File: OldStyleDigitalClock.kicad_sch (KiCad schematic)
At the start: 52 parts, among them SW1 Set minutes, SW2 Set hours, U1 CD4071BM, U10 CD4026BNSR, U2 D168K, U3 CD4026BNSR, U4 D168K, U5 CD4026BNSR, U6 CD4073BM, U7 D168K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

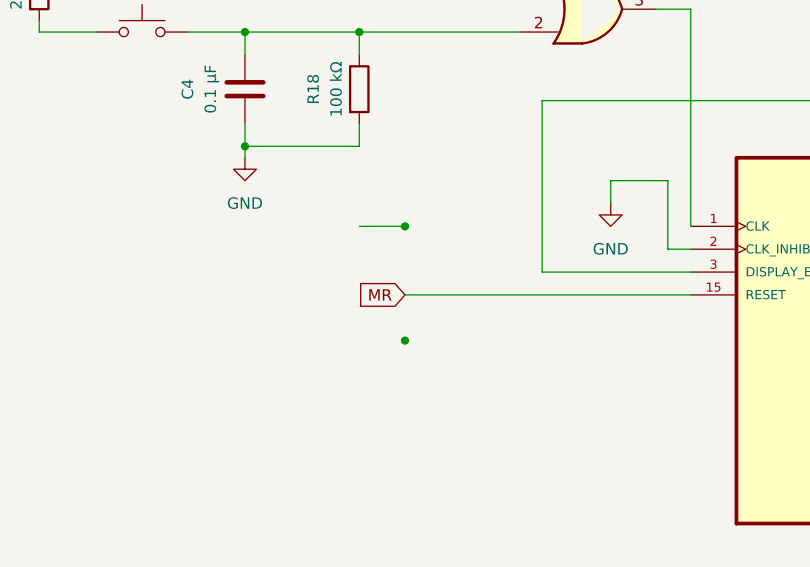
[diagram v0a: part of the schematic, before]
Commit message: Corrected Zener diode specs
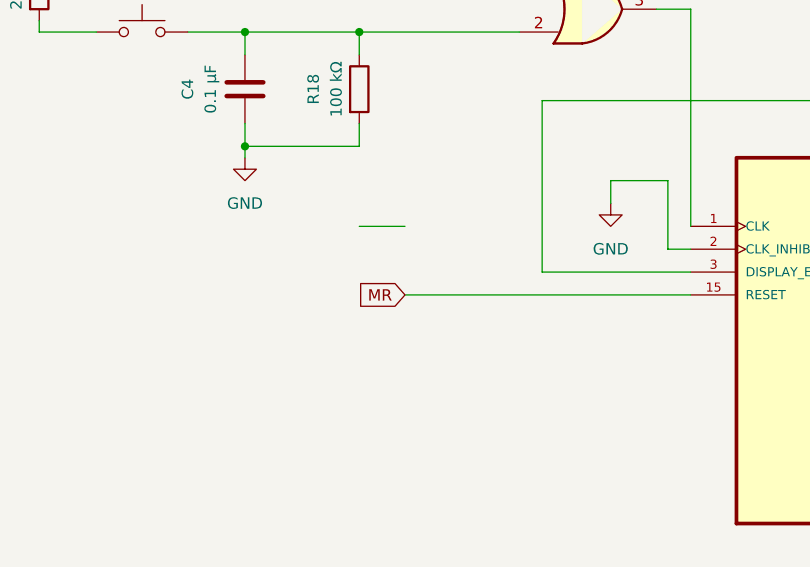
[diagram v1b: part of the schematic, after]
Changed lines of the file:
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@@
-	)
-	(junction
-		(at 134.62 171.45)
-		(diameter 0)
-		(color 0 0 0 0)
 	)
 	(junction
@@
 		(diameter 0)
 		(color 0 0 0 0)
-	)
-	(junction
-		(at 134.62 184.15)
-		(diameter 0)
-		(color 0 0 0 0)

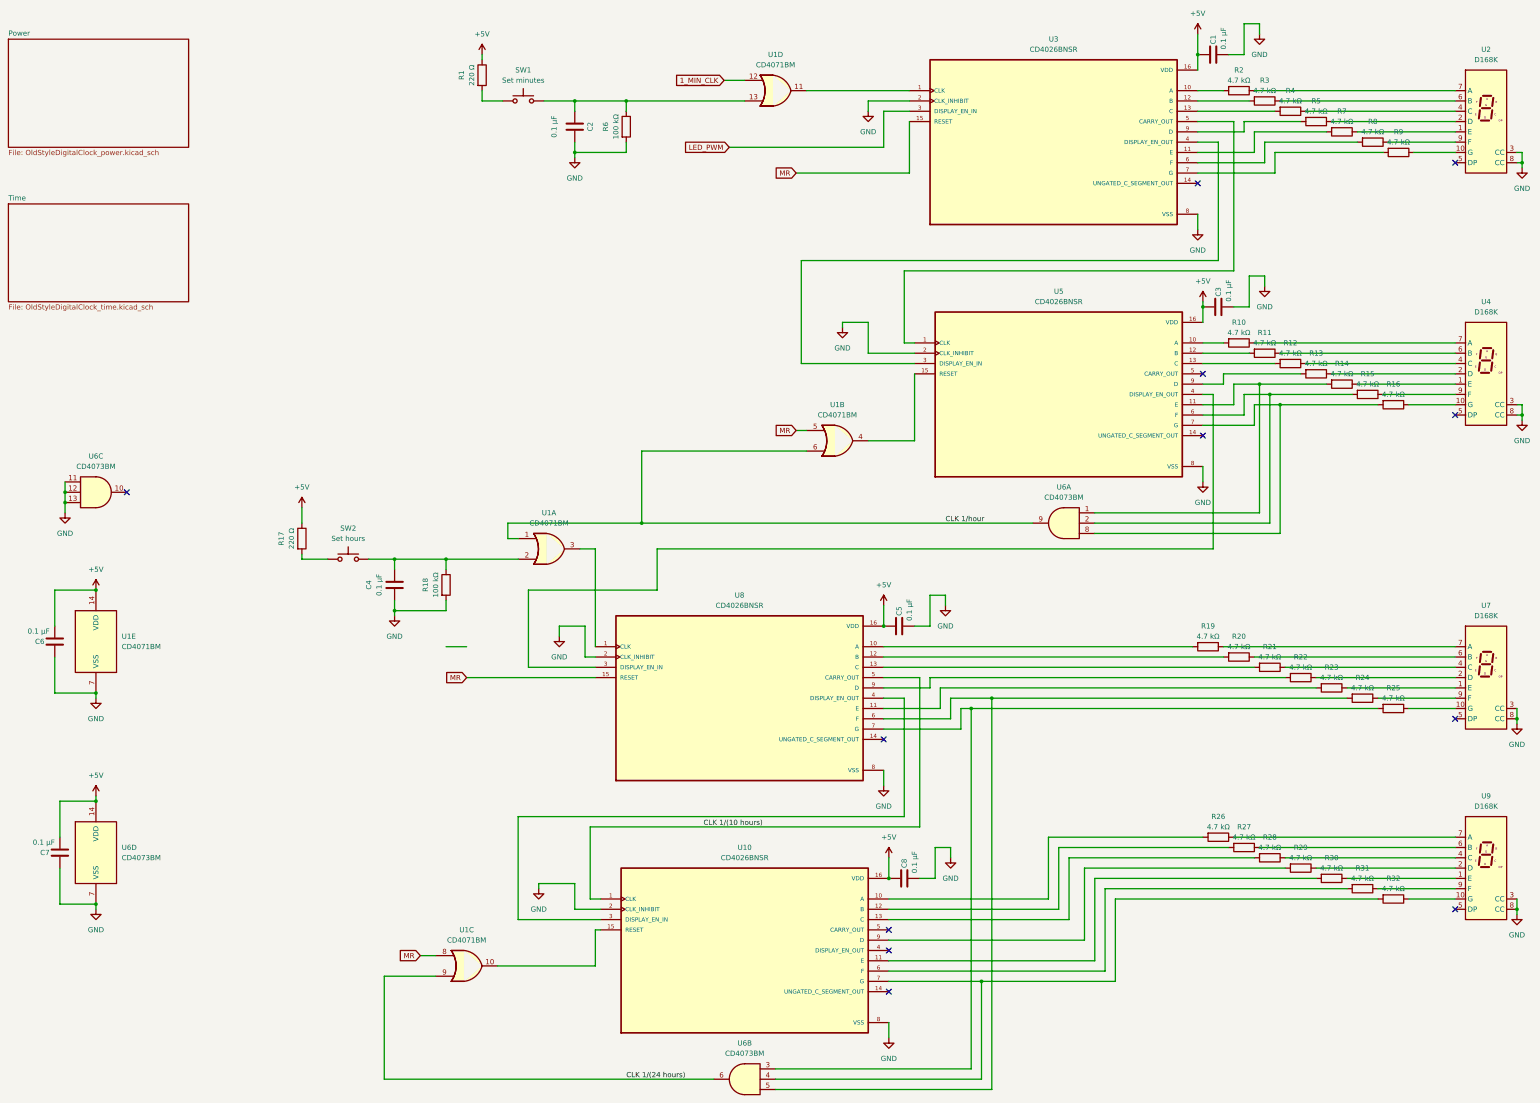
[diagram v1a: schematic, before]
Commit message: Changed units for caps
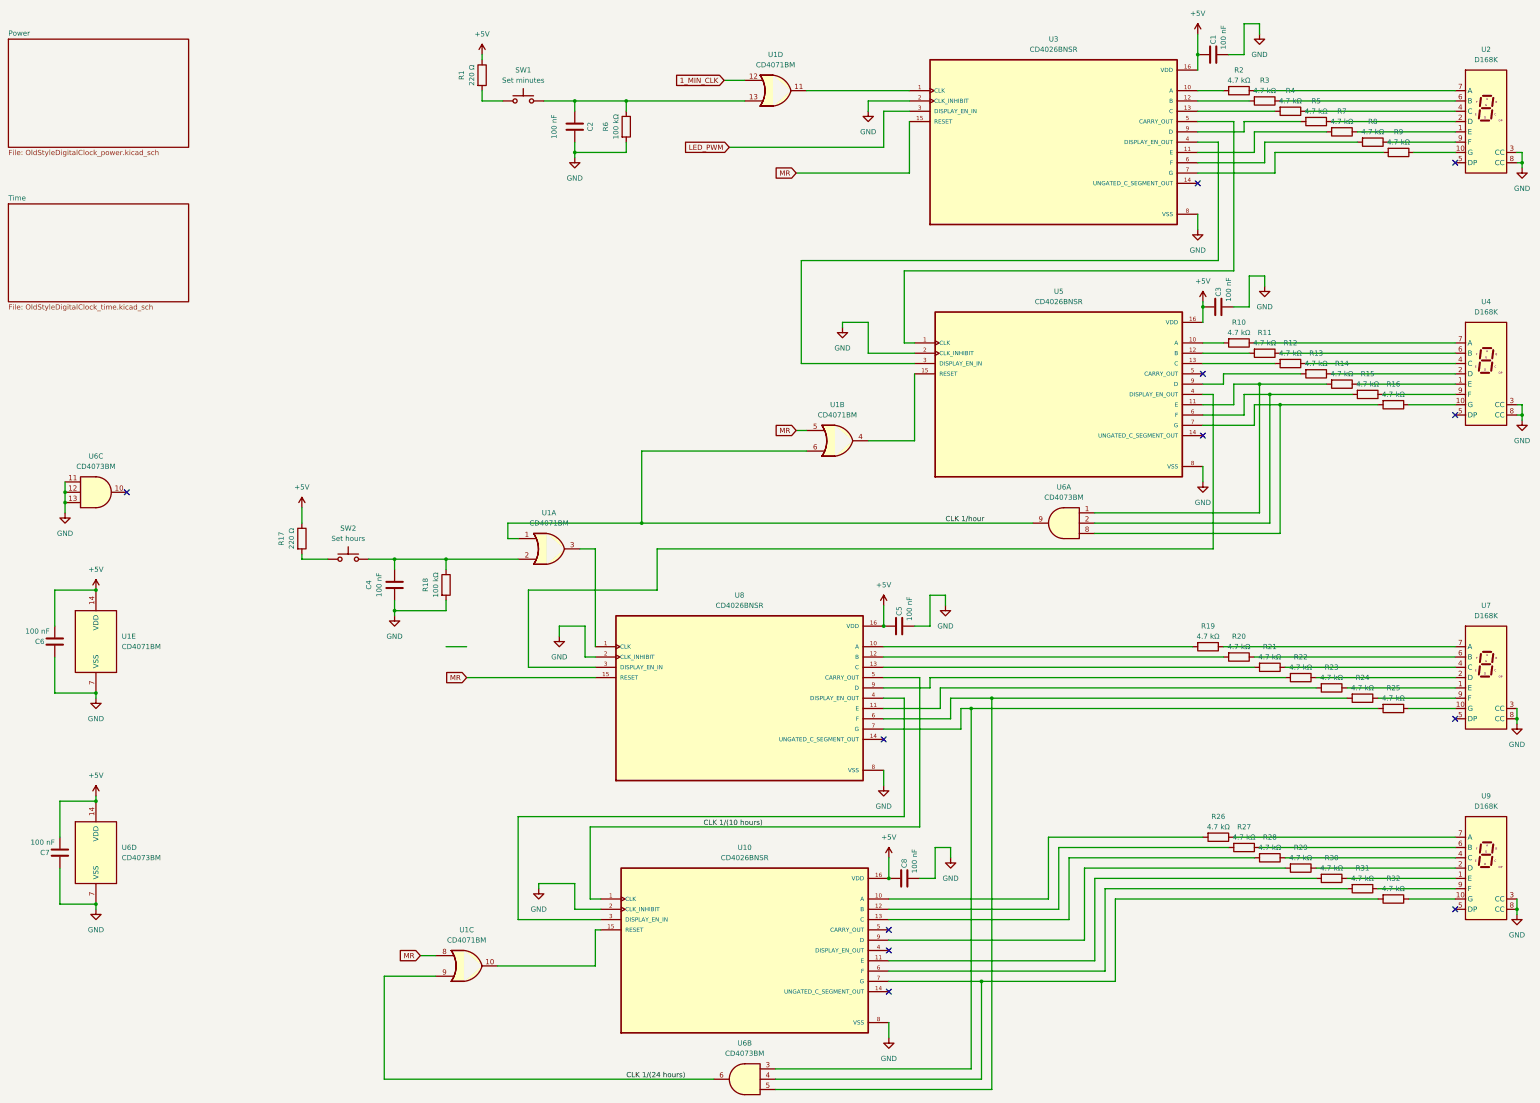
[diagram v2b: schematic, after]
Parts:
- C1, C2, C3, C4, C5, C6, C7, C8: value 0.1 µF -> 100 nF
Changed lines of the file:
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@@
 			)
 		)
-		(property "Value" "0.1 µF"
+		(property "Value" "100 nF"
 			(at 33.02 219.71 0)
 			(effects
@@
 			)
 		)
-		(property "Value" "0.1 µF"
+		(property "Value" "100 nF"
 			(at 156.21 43.18 90)
 			(effects
@@
 			)
 		)
-		(property "Value" "0.1 µF"
+		(property "Value" "100 nF"
 			(at 31.75 167.64 0)
 			(effects
@@
 			)
 		)
-		(property "Value" "0.1 µF"
+		(property "Value" "100 nF"
 			(at 245.11 227.33 0)
 			(effects
@@
 			)
 		)
-		(property "Value" "0.1 µF"
+		(property "Value" "100 nF"
 			(at 243.84 165.1 0)
 			(effects
@@
 			)
 		)
-		(property "Value" "0.1 µF"
+		(property "Value" "100 nF"
 			(at 113.03 156.21 90)
 			(effects
@@
 			)
 		)
-		(property "Value" "0.1 µF"
+		(property "Value" "100 nF"
 			(at 322.58 86.36 0)
 			(effects
@@
 			)
 		)
-		(property "Value" "0.1 µF"
+		(property "Value" "100 nF"
 			(at 321.31 24.13 0)
 			(effects

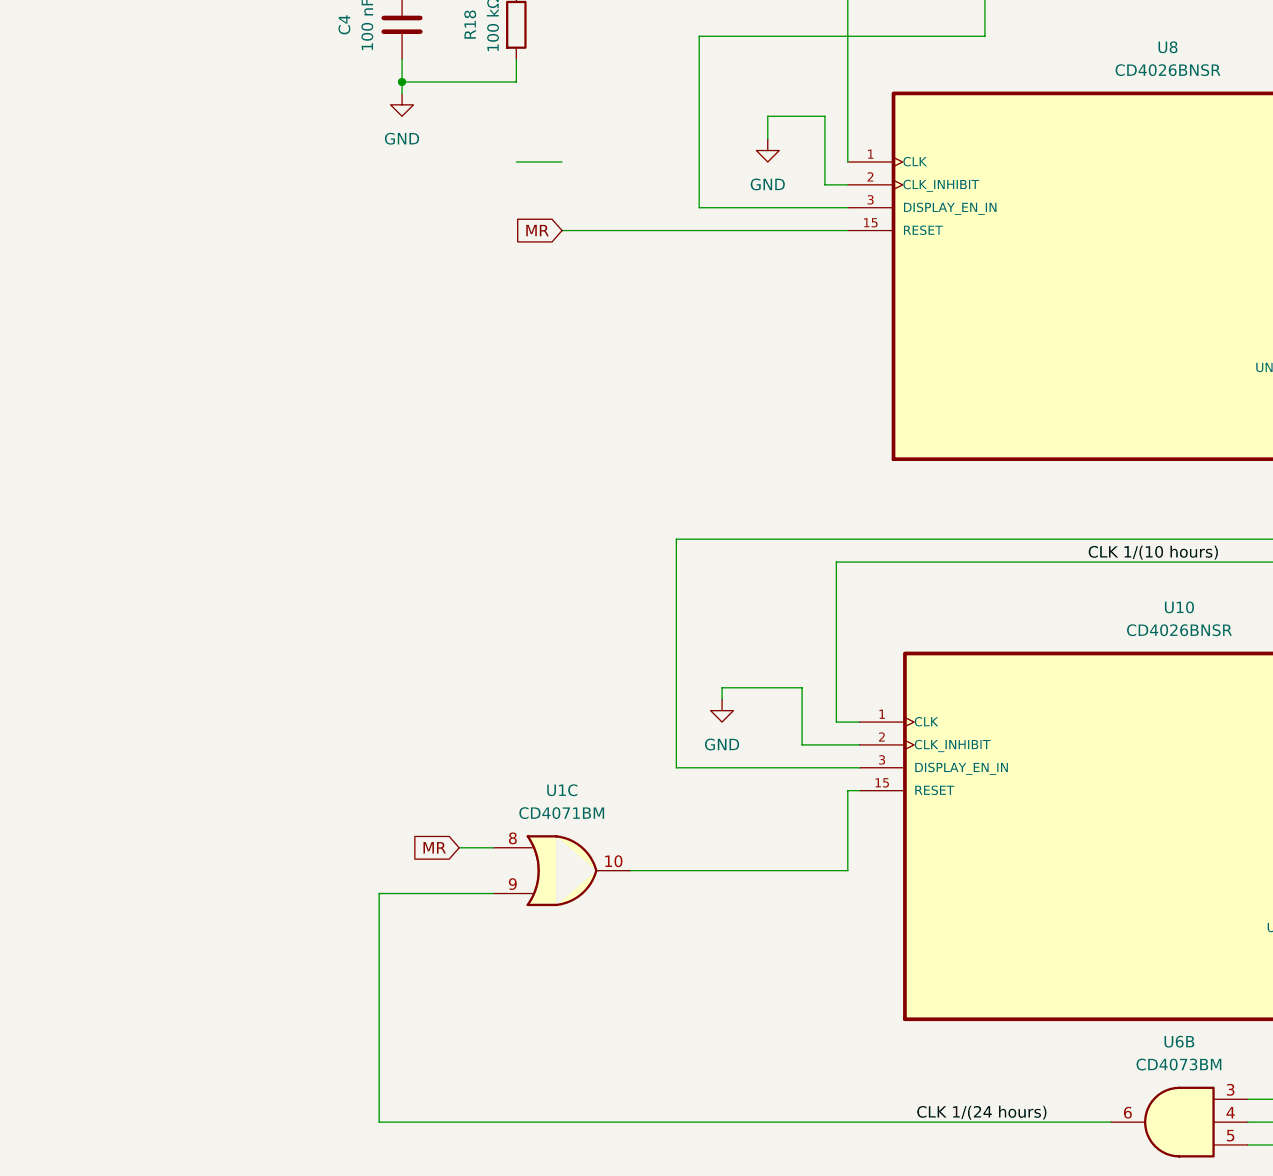
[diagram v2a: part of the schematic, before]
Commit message: Added missing reset connection for low digit of the hours
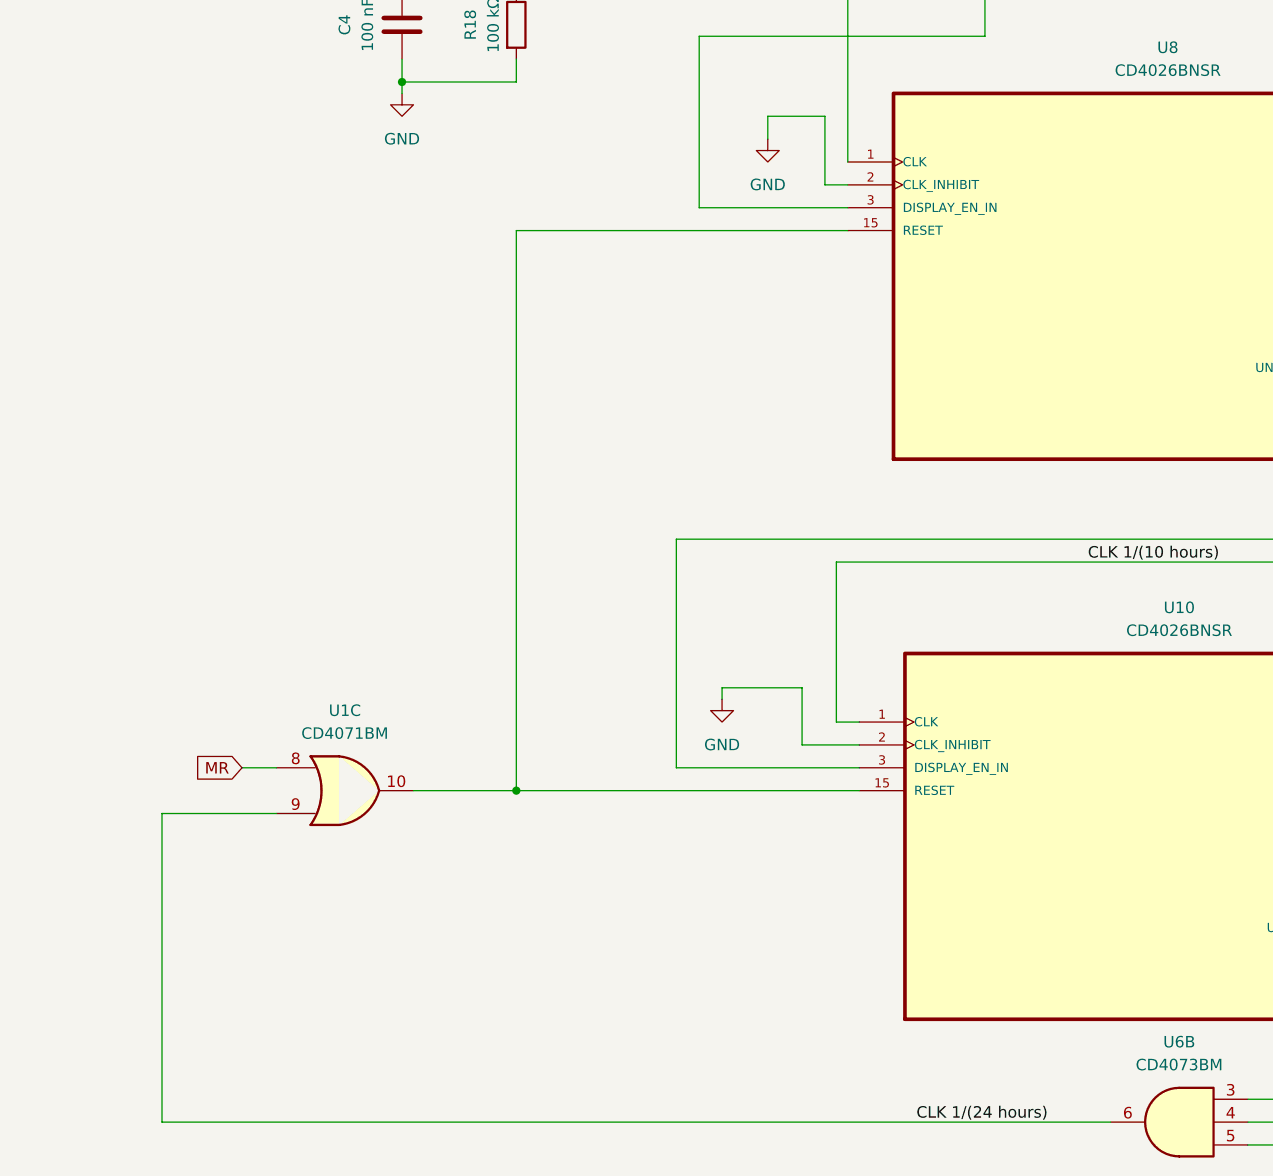
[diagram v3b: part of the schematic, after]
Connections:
- net MR: no longer U8.15 (RESET)
- net at U1.10, U10.15 (RESET): now also U8.15 (RESET)
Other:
- moved on the sheet: U1C
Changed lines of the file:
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@@
+	)
+	(junction
+		(at 129.54 241.3)
+		(diameter 0)
+		(color 0 0 0 0)
 	)
 	(junction
@@
 	(wire
 		(pts
-			(xy 166.37 241.3) (xy 167.64 241.3)
-		)
-		(stroke
-			(width 0)
-			(type default)
-		)
-	)
-	(wire
-		(pts
 			(xy 157.48 166.37) (xy 163.83 166.37)
 		)
@@
 	(wire
 		(pts
+			(xy 129.54 241.3) (xy 129.54 179.07)
+		)
+		(stroke
+			(width 0)
+			(type default)
+		)
+	)
+	(wire
+		(pts
 			(xy 394.97 52.07) (xy 393.7 52.07)
 		)
@@
 	(wire
 		(pts
-			(xy 129.54 171.45) (xy 134.62 171.45)
-		)
-		(stroke
-			(width 0)
-			(type default)
-		)
-	)
-	(wire
-		(pts
 			(xy 246.38 228.6) (xy 250.19 228.6)
 		)
@@
 	(wire
 		(pts
+			(xy 129.54 241.3) (xy 167.64 241.3)
+		)
+		(stroke
+			(width 0)
+			(type default)
+		)
+	)
+	(wire
+		(pts
 			(xy 394.97 114.3) (xy 393.7 114.3)
 		)
@@
 	(wire
 		(pts
-			(xy 166.37 241.3) (xy 166.37 250.19)
-		)
-		(stroke
-			(width 0)
-			(type default)
-		)
-	)
-	(wire
-		(pts
 			(xy 246.38 215.9) (xy 165.1 215.9)
 		)
@@
 	(wire
 		(pts
+			(xy 129.54 179.07) (xy 166.37 179.07)
+		)
+		(stroke
+			(width 0)
+			(type default)
+		)
+	)
+	(wire
+		(pts
 			(xy 328.93 44.45) (xy 346.71 44.45)
 		)
@@
 	(wire
 		(pts
-			(xy 123.19 247.65) (xy 127 247.65)
+			(xy 99.06 238.76) (xy 102.87 238.76)
 		)
 		(stroke
@@
 	(wire
 		(pts
-			(xy 114.3 252.73) (xy 114.3 278.13)
+			(xy 90.17 243.84) (xy 90.17 278.13)
 		)
 		(stroke
@@
 	(wire
 		(pts
-			(xy 114.3 278.13) (xy 195.58 278.13)
+			(xy 90.17 278.13) (xy 195.58 278.13)
 		)
 		(stroke
@@
 	(wire
 		(pts
-			(xy 142.24 250.19) (xy 166.37 250.19)
+			(xy 118.11 241.3) (xy 129.54 241.3)
 		)
 		(stroke
@@
 	(wire
 		(pts
-			(xy 134.62 179.07) (xy 166.37 179.07)
-		)
-		(stroke
-			(width 0)
-			(type default)
-		)
-	)
-	(wire
-		(pts
 			(xy 326.39 25.4) (xy 326.39 17.78)
 		)
@@
 	(wire
 		(pts
-			(xy 114.3 252.73) (xy 127 252.73)
+			(xy 90.17 243.84) (xy 102.87 243.84)
 		)
 		(stroke
@@
 			)
 			(justify left bottom)
-		)
-	)
-	(global_label "MR"
-		(shape input)
-		(at 134.62 179.07 180)
-		(fields_autoplaced yes)
-		(effects
-			(font
-				(size 1.27 1.27)
-			)
-			(justify right)
-		)
-		(property "Intersheetrefs" "${INTERSHEET_REFS}"
-			(at 129.4855 178.9906 0)
-			(effects
-				(font
-					(size 1.27 1.27)
-				)
-				(justify right)
-				(hide yes)
-			)
 		)
 	)
@@
 	(global_label "MR"
 		(shape input)
-		(at 123.19 247.65 180)
+		(at 99.06 238.76 180)
 		(fields_autoplaced yes)
 		(effects
@@
 		)
 		(property "Intersheetrefs" "${INTERSHEET_REFS}"
-			(at 118.0555 247.5706 0)
+			(at 93.9255 238.6806 0)
 			(effects
 				(font
@@
 	(symbol
 		(lib_id "4xxx:4071")
-		(at 134.62 250.19 0)
+		(at 110.49 241.3 0)
 		(unit 3)
 		(exclude_from_sim no)
@@
 		(fields_autoplaced yes)
 		(property "Reference" "U1"
-			(at 134.62 241.3 0)
+			(at 110.49 232.41 0)
 			(effects
 				(font
@@
 		)
 		(property "Value" "CD4071BM"
-			(at 134.62 243.84 0)
+			(at 110.49 234.95 0)
 			(effects
 				(font
@@
 		)
 		(property "Footprint" "Package_SO:SOIC-14_3.9x8.7mm_P1.27mm"
-			(at 134.62 250.19 0)
+			(at 110.49 241.3 0)
 			(effects
 				(font
@@
 		)
 		(property "Datasheet" "https://www.ti.com/lit/ds/symlink/cd4071b.pdf"
-			(at 134.62 250.19 0)
+			(at 110.49 241.3 0)
 			(effects
 				(font
@@
 		)
 		(property "Description" "Quad Or 2 inputs"
-			(at 134.62 250.19 0)
-			(effects
-				(font
+			(at 110.49 241.3 0)
+			(effects
+				(font
